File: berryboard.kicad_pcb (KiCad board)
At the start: 2 copper layers, 0 parts

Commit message: Initialize PCB layout — board outline, mounting holes, all footprints placed
- Added 65×56mm Edge.Cuts board outline (RPi HAT spec)
- Added 4× M2.5 NPTH mounting holes at (3.5,3.5), (3.5,52.5),
  (61.5,3.5), (61.5,52.5) — matches RPi HAT mechanical spec
- Synced schematic netlist to board: all 47 real components placed
  (3 PWR_FLAG symbols correctly excluded from board)
- 12 warnings for JST SH footprint mounting pads (MP) with no net
  assignment — expected/harmless for mechanical pads

Components are currently in a pile at the board origin; placement and
routing are the next steps.

Co-Authored-By: Claude Sonnet 4.6 <noreply@anthropic.com>
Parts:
- added MH1: MountingHole_2.75mm, , F.Cu at (3.50, 3.50)
- added MH2: MountingHole_2.75mm, , F.Cu at (3.50, 52.5)
- added MH3: MountingHole_2.75mm, , F.Cu at (61.5, 3.50)
- added MH4: MountingHole_2.75mm, , F.Cu at (61.5, 52.5)
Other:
- board outline added: 65 x 56 mm
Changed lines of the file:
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@@
 		)
+	)
+	(footprint ""
+		(layer "F.Cu")
+		(at 3.5 3.5)
+		(property "Reference" "MH1"
+			(at 0 0 0)
+			(layer "F.SilkS")
+			(effects
+				(font
+					(size 1.27 1.27)
+				)
+			)
+		)
+		(property "Value" "MountingHole_2.75mm"
+			(at 0 0 0)
+			(layer "F.Fab")
+			(effects
+				(font
+					(size 1.27 1.27)
+				)
+			)
+		)
+		(property "Datasheet" ""
+			(at 0 0 0)
+			(layer "F.Fab")
+			(hide yes)
+			(effects
+				(font
+					(size 1.27 1.27)
+				)
+			)
+		)
+		(property "Description" ""
+			(at 0 0 0)
+			(layer "F.Fab")
+			(hide yes)
+			(effects
+				(font
+					(size 1.27 1.27)
+				)
+			)
+		)
+		(duplicate_pad_numbers_are_jumpers no)
+		(pad "" np_thru_hole circle
+			(at 0 0)
+			(size 3.75 3.75)
+			(drill 2.75)
+			(layers "*.Cu" "*.Mask")
+		)
+		(embedded_fonts no)
+	)
+	(footprint ""
+		(layer "F.Cu")
+		(at 61.5 3.5)
+		(property "Reference" "MH3"
+			(at 0 0 0)
+			(layer "F.SilkS")
+			(effects
+				(font
+					(size 1.27 1.27)
+				)
+			)
+		)
+		(property "Value" "MountingHole_2.75mm"
+			(at 0 0 0)
+			(layer "F.Fab")
+			(effects
+				(font
+					(size 1.27 1.27)
+				)
+			)
+		)
+		(property "Datasheet" ""
+			(at 0 0 0)
+			(layer "F.Fab")
+			(hide yes)
+			(effects
+				(font
+					(size 1.27 1.27)
+				)
+			)
+		)
+		(property "Description" ""
+			(at 0 0 0)
+			(layer "F.Fab")
+			(hide yes)
+			(effects
+				(font
+					(size 1.27 1.27)
+				)
+			)
+		)
+		(duplicate_pad_numbers_are_jumpers no)
+		(pad "" np_thru_hole circle
+			(at 0 0)
+			(size 3.75 3.75)
+			(drill 2.75)
+			(layers "*.Cu" "*.Mask")
+		)
+		(embedded_fonts no)
+	)
+	(footprint ""
+		(layer "F.Cu")
+		(at 3.5 52.5)
+		(property "Reference" "MH2"
+			(at 0 0 0)
+			(layer "F.SilkS")
+			(effects
+				(font
+					(size 1.27 1.27)
+				)
+			)
+		)
+		(property "Value" "MountingHole_2.75mm"
+			(at 0 0 0)
+			(layer "F.Fab")
+			(effects
+				(font
+					(size 1.27 1.27)
+				)
+			)
+		)
+		(property "Datasheet" ""
+			(at 0 0 0)
+			(layer "F.Fab")
+			(hide yes)
+			(effects
+				(font
+					(size 1.27 1.27)
+				)
+			)
+		)
+		(property "Description" ""
+			(at 0 0 0)
+			(layer "F.Fab")
+			(hide yes)
+			(effects
+				(font
+					(size 1.27 1.27)
+				)
+			)
+		)
+		(duplicate_pad_numbers_are_jumpers no)
+		(pad "" np_thru_hole circle
+			(at 0 0)
+			(size 3.75 3.75)
+			(drill 2.75)
+			(layers "*.Cu" "*.Mask")
+		)
+		(embedded_fonts no)
+	)
+	(footprint ""
+		(layer "F.Cu")
+		(at 61.5 52.5)
+		(property "Reference" "MH4"
+			(at 0 0 0)
+			(layer "F.SilkS")
+			(effects
+				(font
+					(size 1.27 1.27)
+				)
+			)
+		)
+		(property "Value" "MountingHole_2.75mm"
+			(at 0 0 0)
+			(layer "F.Fab")
+			(effects
+				(font
+					(size 1.27 1.27)
+				)
+			)
+		)
+		(property "Datasheet" ""
+			(at 0 0 0)
+			(layer "F.Fab")
+			(hide yes)
+			(effects
+				(font
+					(size 1.27 1.27)
+				)
+			)
+		)
+		(property "Description" ""
+			(at 0 0 0)
+			(layer "F.Fab")
+			(hide yes)
+			(effects
+				(font
+					(size 1.27 1.27)
+				)
+			)
+		)
+		(duplicate_pad_numbers_are_jumpers no)
+		(pad "" np_thru_hole circle
+			(at 0 0)
+			(size 3.75 3.75)
+			(drill 2.75)
+			(layers "*.Cu" "*.Mask")
+		)
+		(embedded_fonts no)
+	)
+	(gr_line
+		(start 0 0)
+		(end 65 0)
+		(stroke
+			(width 0)
+			(type default)
+		)
+		(layer "Edge.Cuts")
+	)
+	(gr_line
+		(start 0 56)
+		(end 0 0)
+		(stroke
+			(width 0)
+			(type default)
+		)
+		(layer "Edge.Cuts")
+	)
+	(gr_line
+		(start 65 0)
+		(end 65 56)
+		(stroke
+			(width 0)
+			(type default)
+		)
+		(layer "Edge.Cuts")
+	)
+	(gr_line
+		(start 65 56)
+		(end 0 56)
+		(stroke
+			(width 0)
+			(type default)
+		)
+		(layer "Edge.Cuts")
 	)
 	(embedded_fonts no)

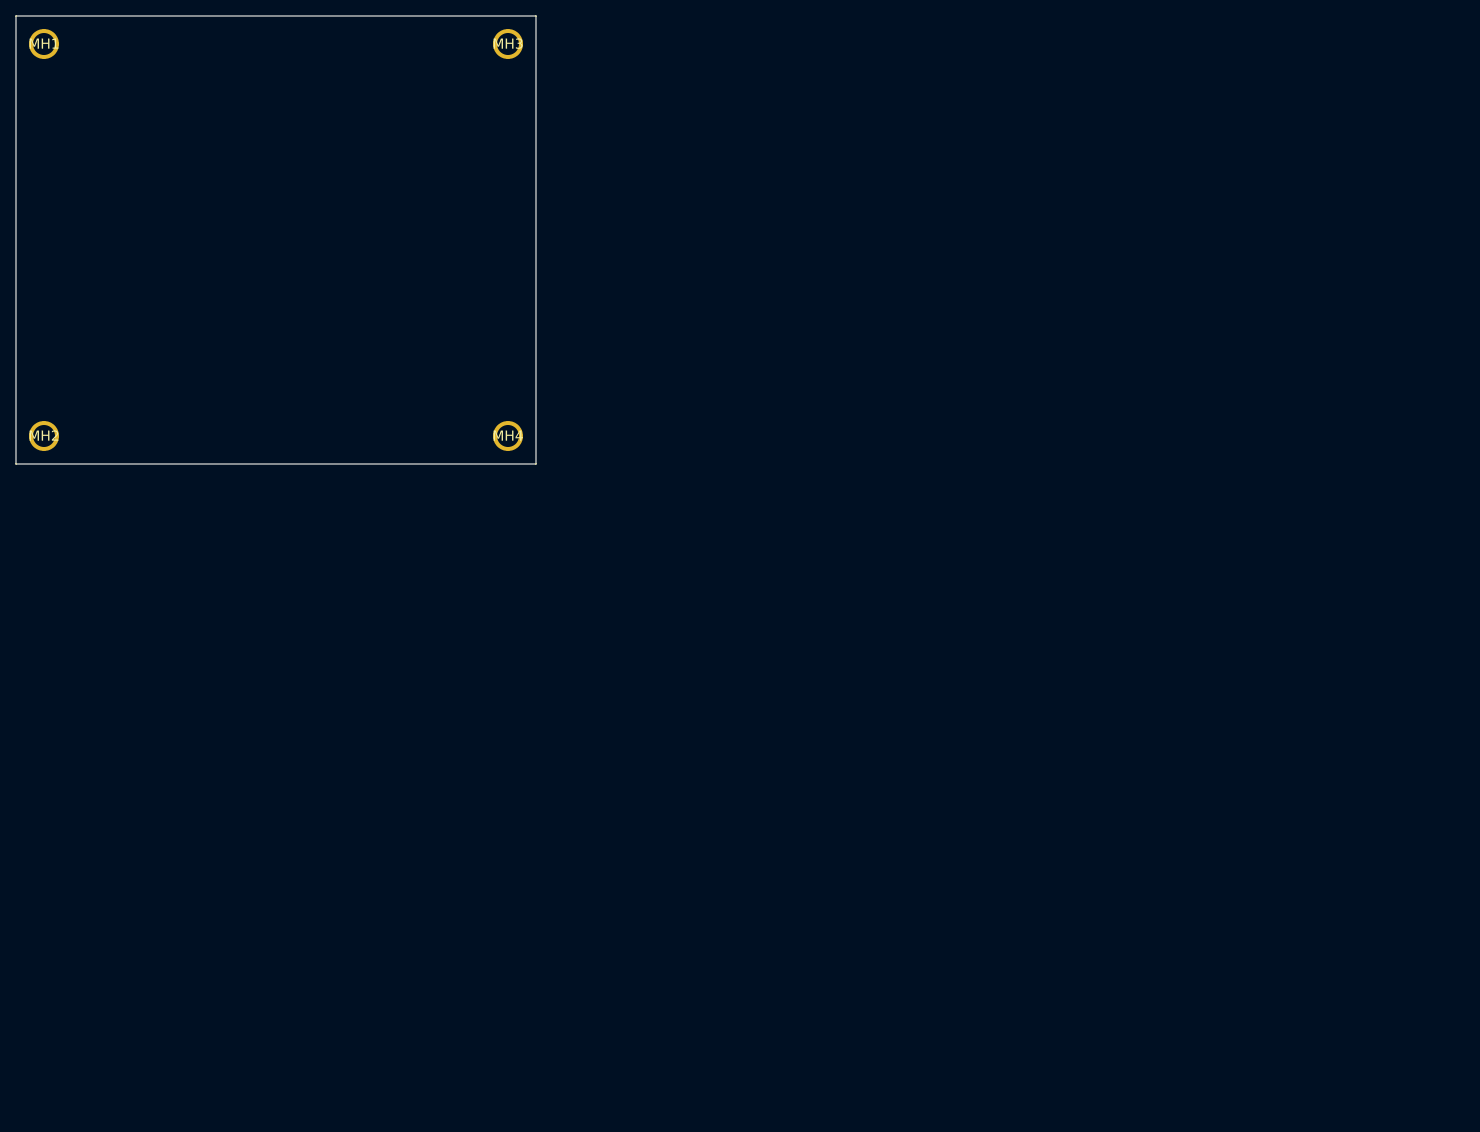
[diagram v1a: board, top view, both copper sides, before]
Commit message: Center board outline on A4 page
Move Edge.Cuts rectangle and mounting holes from (0,0) origin to
(116,77)-(181,133), centering the 65×56mm HAT on the 297×210mm A4 page.

Co-Authored-By: Claude Sonnet 4.6 <noreply@anthropic.com>
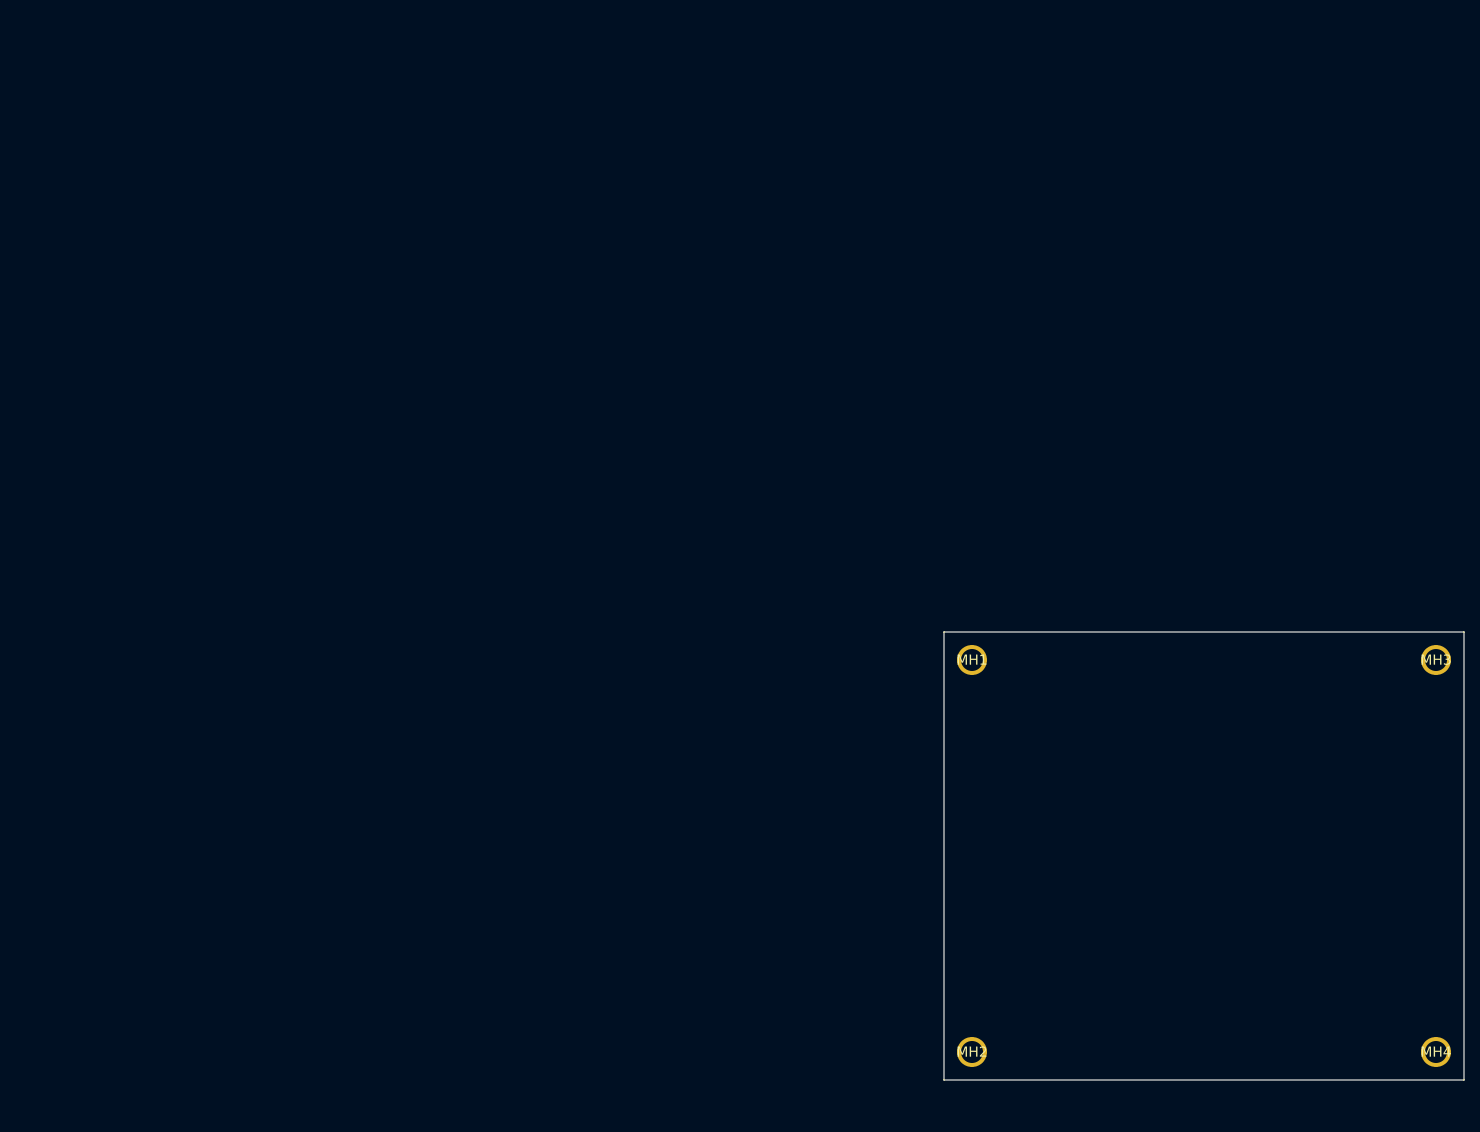
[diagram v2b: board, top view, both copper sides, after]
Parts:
- moved MH1 139.2 mm to (119.5, 80.5)
- moved MH2 139.2 mm to (119.5, 129.5)
- moved MH3 139.2 mm to (177.5, 80.5)
- moved MH4 139.2 mm to (177.5, 129.5)
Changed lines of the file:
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@@
 	(footprint ""
 		(layer "F.Cu")
-		(at 3.5 3.5)
+		(at 119.5 80.5)
 		(property "Reference" "MH1"
 			(at 0 0 0)
@@
 	(footprint ""
 		(layer "F.Cu")
-		(at 61.5 3.5)
+		(at 177.5 80.5)
 		(property "Reference" "MH3"
 			(at 0 0 0)
@@
 	(footprint ""
 		(layer "F.Cu")
-		(at 3.5 52.5)
+		(at 119.5 129.5)
 		(property "Reference" "MH2"
 			(at 0 0 0)
@@
 	(footprint ""
 		(layer "F.Cu")
-		(at 61.5 52.5)
+		(at 177.5 129.5)
 		(property "Reference" "MH4"
 			(at 0 0 0)
@@
 	)
 	(gr_line
-		(start 0 0)
-		(end 65 0)
+		(start 116 77)
+		(end 181 77)
 		(stroke
 			(width 0)
@@
 	)
 	(gr_line
-		(start 0 56)
-		(end 0 0)
+		(start 116 133)
+		(end 116 77)
 		(stroke
 			(width 0)
@@
 	)
 	(gr_line
-		(start 65 0)
-		(end 65 56)
+		(start 181 77)
+		(end 181 133)
 		(stroke
 			(width 0)
@@
 	)
 	(gr_line
-		(start 65 56)
-		(end 0 56)
-		(stroke
-			(width 0)
+		(start 181 133)
+		(end 116 133)
+		(stroke
+			(width 0)

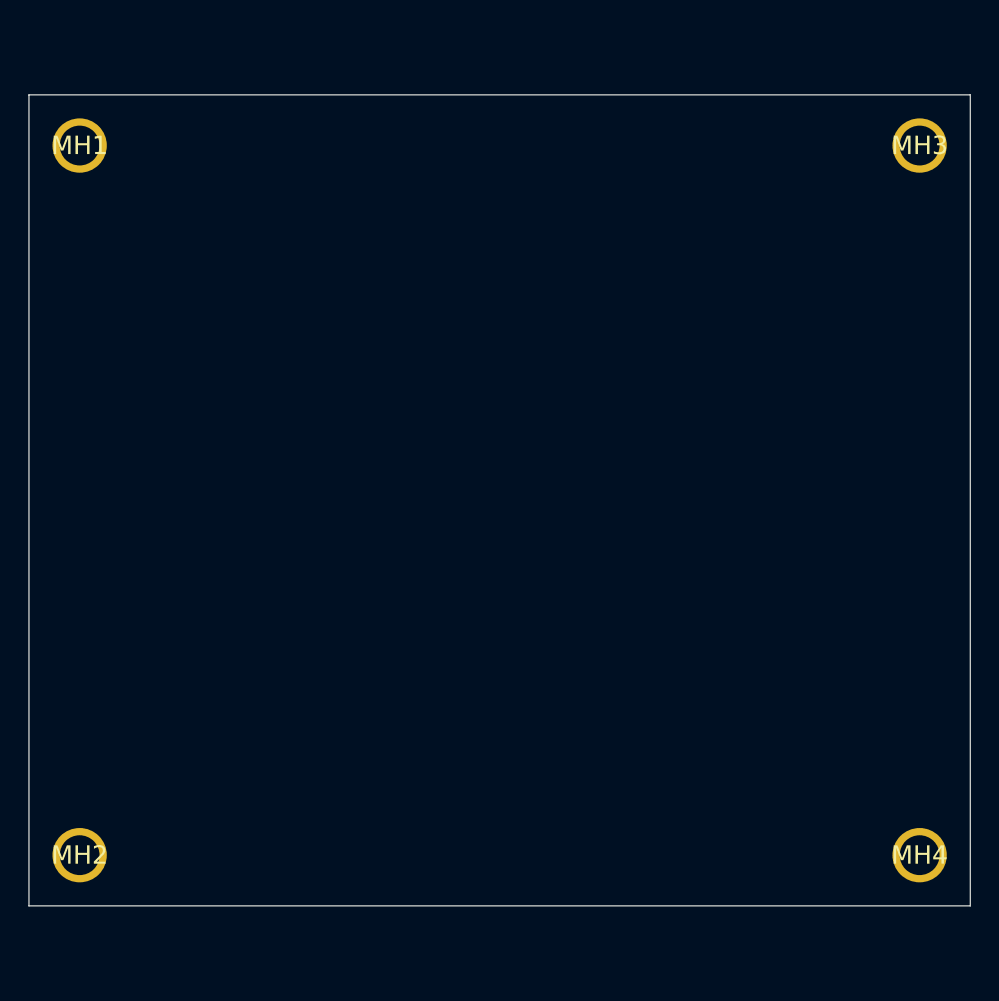
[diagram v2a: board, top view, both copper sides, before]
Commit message: Rotate board 90° — 56mm wide × 65mm tall, recentered on A4 page
The GPIO header (J2) runs along the long (65mm) axis, so the board
must be portrait orientation (56×65) not landscape (65×56).

Board outline: (120.5, 72.5) – (176.5, 137.5) on A4 page
Mounting holes: (124,76), (173,76), (124,134), (173,134)
  — still 3.5mm from each corner per RPi HAT+ spec

Co-Authored-By: Claude Sonnet 4.6 <noreply@anthropic.com>
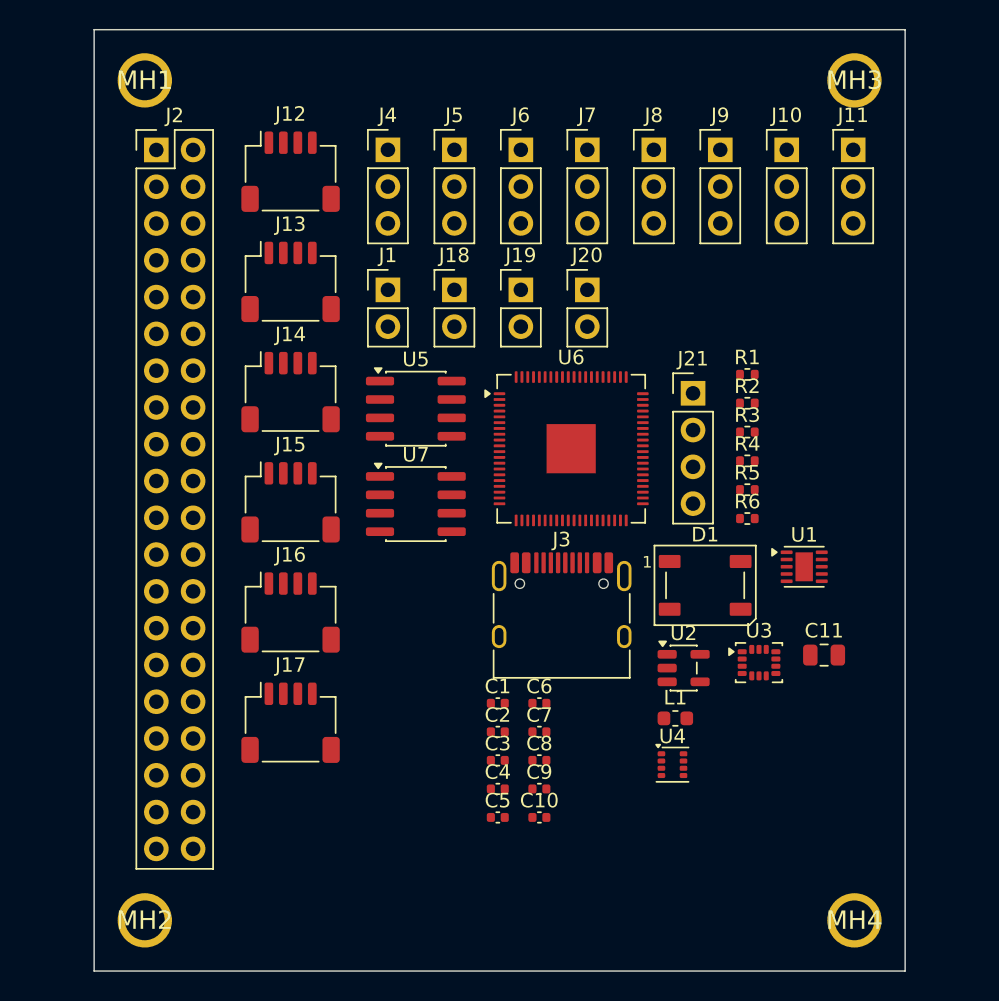
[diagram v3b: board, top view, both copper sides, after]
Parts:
- added C1: 100nF, Capacitor_SMD:C_0402_1005Metric, F.Cu at (148.4, 119.0)
- added C10: 10uF, Capacitor_SMD:C_0402_1005Metric, F.Cu at (151.2, 126.9)
- added C11: 47uF, Capacitor_SMD:C_0805_2012Metric, F.Cu at (170.9, 115.7)
- added C2: 100nF, Capacitor_SMD:C_0402_1005Metric, F.Cu at (148.4, 121.0)
- added C3: 10uF, Capacitor_SMD:C_0402_1005Metric, F.Cu at (148.4, 123.0)
- added C4: 100nF, Capacitor_SMD:C_0402_1005Metric, F.Cu at (148.4, 124.9)
- added C5: 100nF, Capacitor_SMD:C_0402_1005Metric, F.Cu at (148.4, 126.9)
- added C6: 100nF, Capacitor_SMD:C_0402_1005Metric, F.Cu at (151.2, 119.0)
- added C7: 100nF, Capacitor_SMD:C_0402_1005Metric, F.Cu at (151.2, 121.0)
- added C8: 100nF, Capacitor_SMD:C_0402_1005Metric, F.Cu at (151.2, 123.0)
- added C9: 100nF, Capacitor_SMD:C_0402_1005Metric, F.Cu at (151.2, 124.9)
- added D1: WS2812B, LED_SMD:LED_WS2812B_PLCC4_5.0x5.0mm_P3.2mm, F.Cu at (162.7, 110.9)
- added J1: XT30_SERVO_PWR, Connector_PinHeader_2.54mm:PinHeader_1x02_P2.54mm_Vertical, F.Cu at (140.8, 90.5)
- added J10: SERVO_7, Connector_PinHeader_2.54mm:PinHeader_1x03_P2.54mm_Vertical, F.Cu at (168.3, 80.8)
- added J11: SERVO_8, Connector_PinHeader_2.54mm:PinHeader_1x03_P2.54mm_Vertical, F.Cu at (172.9, 80.8)
- added J12: QWIIC_RPI_1, Connector_JST:JST_SH_SM04B-SRSS-TB_1x04-1MP_P1.00mm_Horizontal, F.Cu at (134.1, 82.3)
- added J13: QWIIC_RPI_2, Connector_JST:JST_SH_SM04B-SRSS-TB_1x04-1MP_P1.00mm_Horizontal, F.Cu at (134.1, 89.9)
- added J14: QWIIC_RPI_3, Connector_JST:JST_SH_SM04B-SRSS-TB_1x04-1MP_P1.00mm_Horizontal, F.Cu at (134.1, 97.5)
- added J15: QWIIC_MCU_1, Connector_JST:JST_SH_SM04B-SRSS-TB_1x04-1MP_P1.00mm_Horizontal, F.Cu at (134.1, 105.1)
- added J16: QWIIC_MCU_2, Connector_JST:JST_SH_SM04B-SRSS-TB_1x04-1MP_P1.00mm_Horizontal, F.Cu at (134.1, 112.7)
- added J17: QWIIC_MCU_3, Connector_JST:JST_SH_SM04B-SRSS-TB_1x04-1MP_P1.00mm_Horizontal, F.Cu at (134.1, 120.4)
- added J18: LEAK_1, Connector_PinHeader_2.54mm:PinHeader_1x02_P2.54mm_Vertical, F.Cu at (145.4, 90.5)
- added J19: LEAK_2, Connector_PinHeader_2.54mm:PinHeader_1x02_P2.54mm_Vertical, F.Cu at (150.0, 90.5)
- added J2: RPi_GPIO_40P, Connector_PinHeader_2.54mm:PinHeader_2x20_P2.54mm_Vertical, F.Cu at (124.8, 80.8)
- added J20: HAT_5V_IN, Connector_PinHeader_2.54mm:PinHeader_1x02_P2.54mm_Vertical, F.Cu at (154.6, 90.5)
- added J21: SWD, Connector_PinHeader_2.54mm:PinHeader_1x04_P2.54mm_Vertical, F.Cu at (161.9, 97.6)
- added J3: USB_C_RP2350, Connector_USB:USB_C_Receptacle_HRO_TYPE-C-31-M-12, F.Cu at (152.8, 113.4)
- added J4: SERVO_1, Connector_PinHeader_2.54mm:PinHeader_1x03_P2.54mm_Vertical, F.Cu at (140.8, 80.8)
- added J5: SERVO_2, Connector_PinHeader_2.54mm:PinHeader_1x03_P2.54mm_Vertical, F.Cu at (145.4, 80.8)
- added J6: SERVO_3, Connector_PinHeader_2.54mm:PinHeader_1x03_P2.54mm_Vertical, F.Cu at (150.0, 80.8)
- added J7: SERVO_4, Connector_PinHeader_2.54mm:PinHeader_1x03_P2.54mm_Vertical, F.Cu at (154.6, 80.8)
- added J8: SERVO_5, Connector_PinHeader_2.54mm:PinHeader_1x03_P2.54mm_Vertical, F.Cu at (159.1, 80.8)
- added J9: SERVO_6, Connector_PinHeader_2.54mm:PinHeader_1x03_P2.54mm_Vertical, F.Cu at (163.7, 80.8)
- added L1: 10uH, Inductor_SMD:L_0603_1608Metric, F.Cu at (160.6, 120.1)
- added R1: 5.1k, Resistor_SMD:R_0402_1005Metric, F.Cu at (165.6, 96.3)
- added R2: 5.1k, Resistor_SMD:R_0402_1005Metric, F.Cu at (165.6, 98.3)
- added R3: 4.7k, Resistor_SMD:R_0402_1005Metric, F.Cu at (165.6, 100.3)
- added R4: 4.7k, Resistor_SMD:R_0402_1005Metric, F.Cu at (165.6, 102.3)
- added R5: 4.7k, Resistor_SMD:R_0402_1005Metric, F.Cu at (165.6, 104.3)
- added R6: 4.7k, Resistor_SMD:R_0402_1005Metric, F.Cu at (165.6, 106.3)
- added U1: TPS2121, Package_SON:WSON-10-1EP_2.5x2.5mm_P0.5mm_EP1.2x2mm, F.Cu at (169.5, 109.6)
- added U2: AP2112K-3.3, Package_TO_SOT_SMD:SOT-23-5, F.Cu at (161.2, 116.6)
- added U3: ICM-42688-P, Package_LGA:LGA-14_3x2.5mm_P0.5mm_LayoutBorder3x4y, F.Cu at (166.4, 116.2)
- added U4: MMC5983MA, OptoDevice:Broadcom_LGA-8_2x2mm_P0.5mm, F.Cu at (160.4, 123.2)
- added U5: 24LC32, Package_SO:SOIC-8_3.9x4.9mm_P1.27mm, F.Cu at (142.7, 98.7)
- added U6: RP2350B, Package_DFN_QFN:QFN-80-1EP_10x10mm_P0.4mm_EP3.4x3.4mm, F.Cu at (153.4, 101.4)
- added U7: W25Q16JVSS, Package_SO:SOIC-8_3.9x4.9mm_P1.27mm, F.Cu at (142.7, 105.3)
- moved MH1 6.36 mm to (124.0, 76.0)
- moved MH2 6.36 mm to (124.0, 134.0)
- moved MH3 6.36 mm to (173.0, 76.0)
- moved MH4 6.36 mm to (173.0, 134.0)
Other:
- board size 65 x 56 mm -> 56 x 65 mm
